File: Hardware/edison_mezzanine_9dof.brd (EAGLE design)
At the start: 30.5 x 44.5 mm, 43 parts, among them U1 LSM9DS0, U2 EDISON_CONNECTOR_FULLMOUNTING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, U3 EDISON_CONNECTOR_FULLHEADER, U4 MIC52053.3V

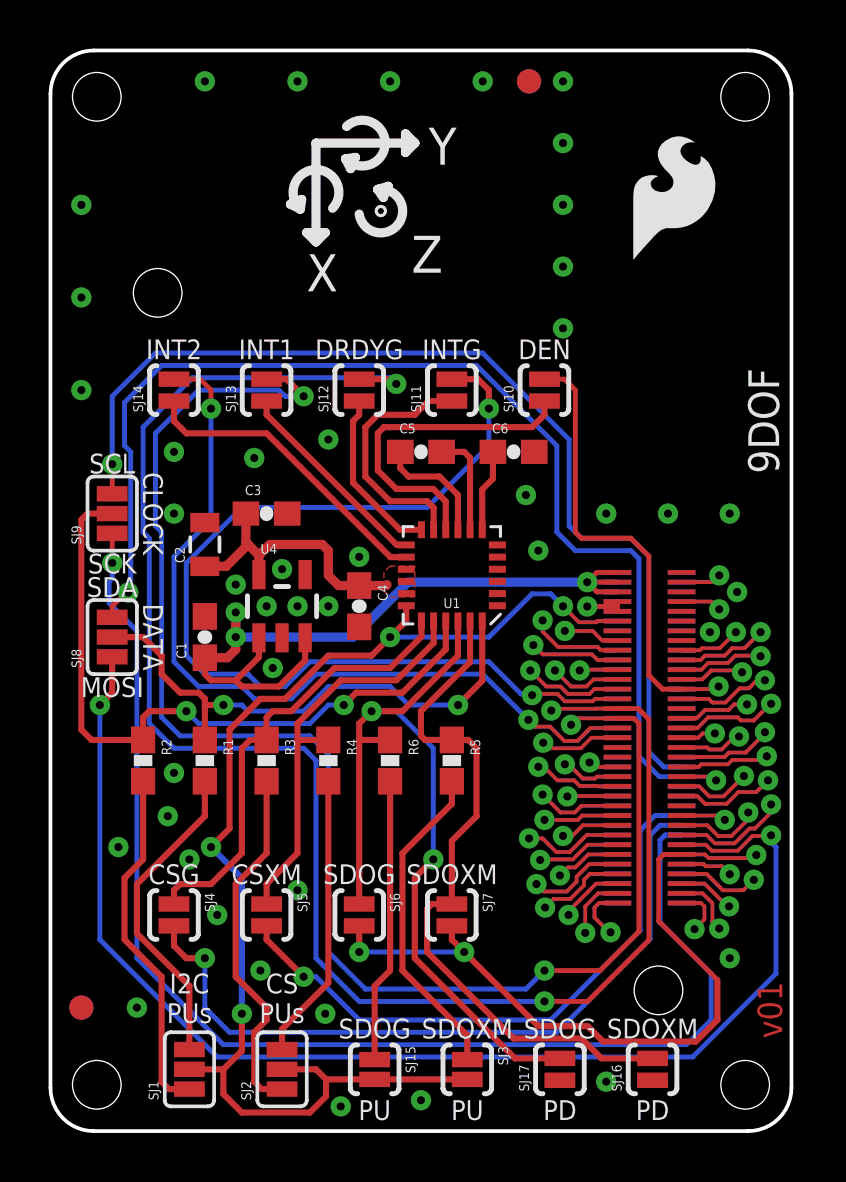
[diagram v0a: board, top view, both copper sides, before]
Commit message: Added DCIN pin Corrected Header footprint Modified Name of board cleaned up units and added units cleaned up copper fills
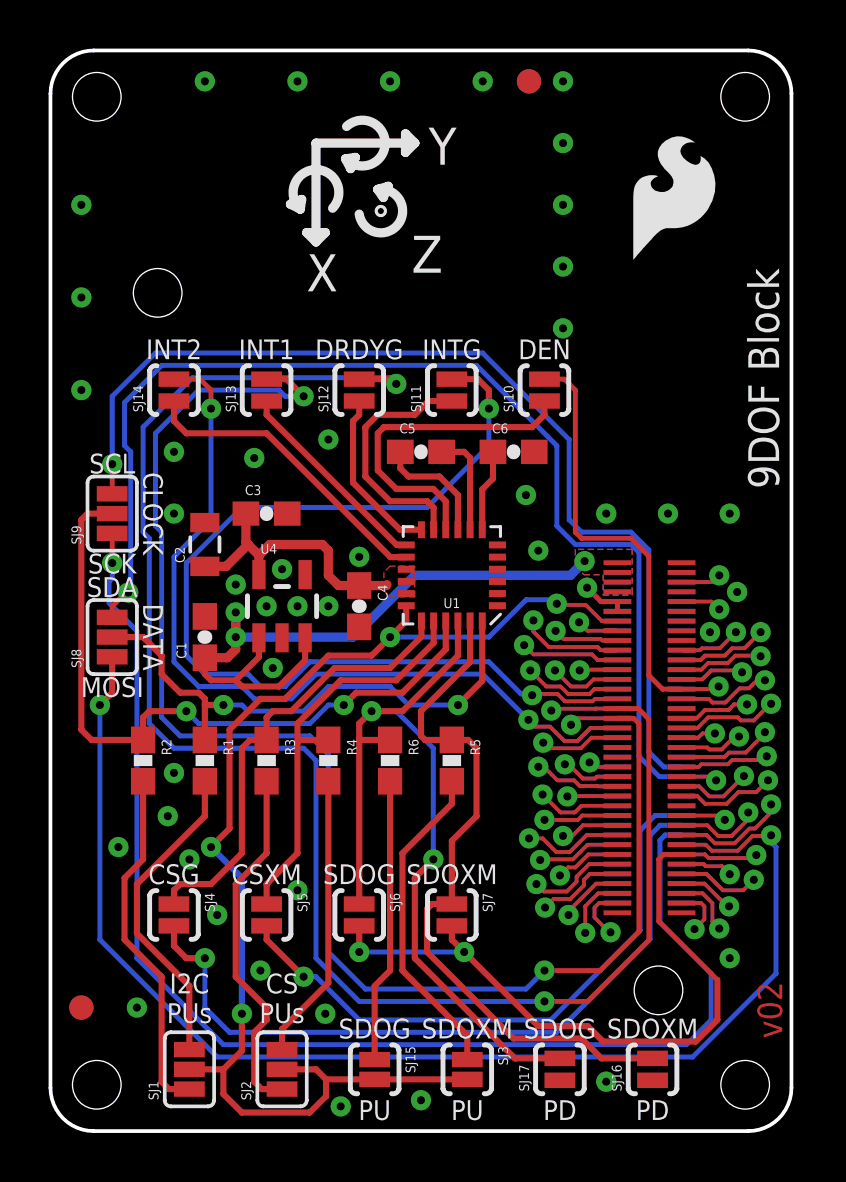
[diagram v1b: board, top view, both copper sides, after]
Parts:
- removed FRAME3: FRAME-LETTER, SparkFun-Aesthetics:CREATIVE_COMMONS
- R1, R2: value 4.7k -> DNP
- moved FRAME1 10.2 mm to (0.00, -15.2)
- moved FRAME2 10.2 mm to (0.00, -15.2)
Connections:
- new net DCIN: U2.14, U3.14
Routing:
- net VSYS: track 36.1 -> 28.3 mm
- net DCIN: track 0.00 -> 3.44 mm, vias 0 -> 1
- net USB_DP: track 4.65 -> 5.41 mm
- net USB_VBUS: track 7.42 -> 8.18 mm
- net USB_DN: track 7.70 -> 8.47 mm
- added copper zone on layer 1, net VSYS
- added copper zone on layer 16, net VSYS
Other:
- board text added: "9DOF Block"
- board text added: "NOTE: Units are in Inches"
- board text added: "v02"
- board text removed: "9DOF"
- board text removed: "Connectors Go Here"
- board text removed: "LED's and selector switches go here"
- board text removed: "Max Board Length"
- board text removed: "Nothing goes here... I mean it."
- board text removed: "v01"

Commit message: Rev to 10, fix gnd and pwr, text
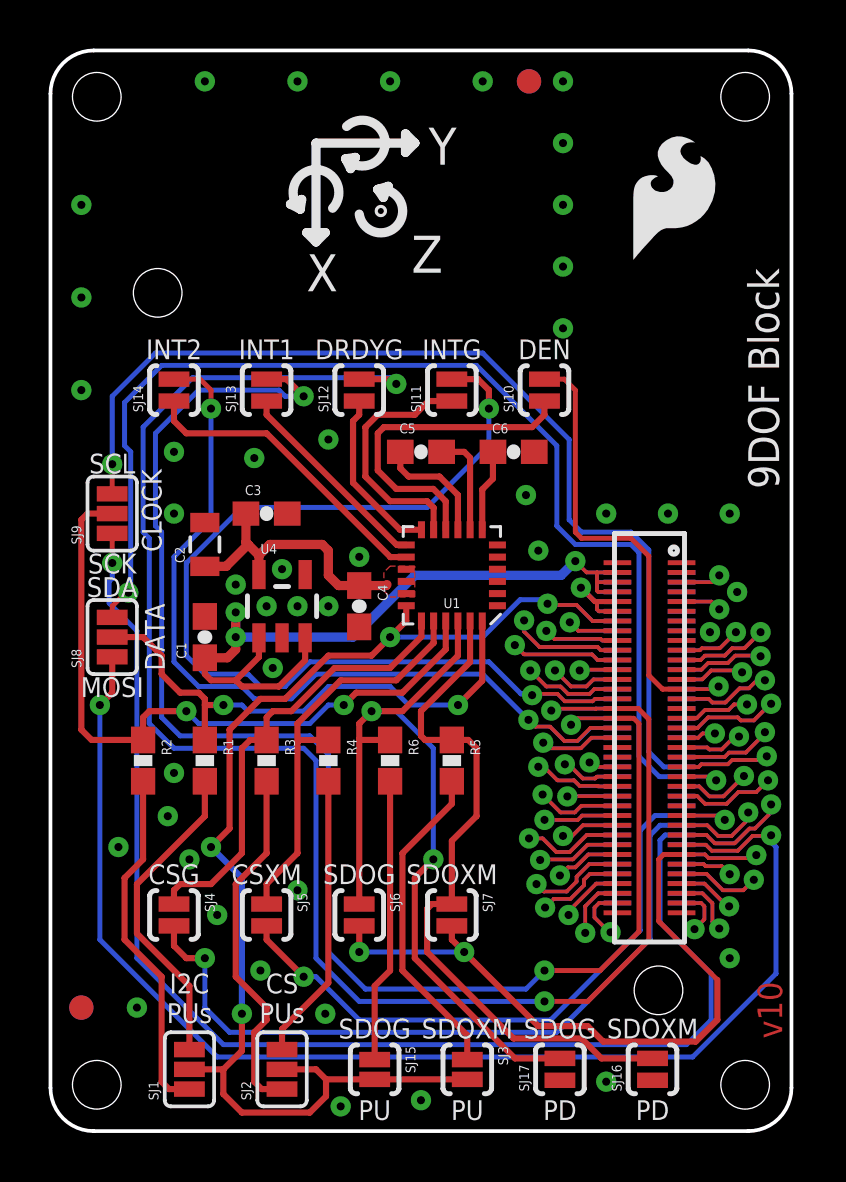
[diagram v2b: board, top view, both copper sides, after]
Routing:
- net VSYS: track 28.3 -> 36.7 mm
- net 3.3V: track 4.17 -> 5.97 mm
- net USB_VBUS: track 8.18 -> 8.94 mm
- net USB_DN: track 8.47 -> 9.23 mm
- net DCIN: track 3.44 -> 4.21 mm
- net USB_DP: track 5.41 -> 6.17 mm
- removed copper zone on layer 1, net VSYS
- removed copper zone on layer 16, net VSYS
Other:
- board text added: "v10"
- board text removed: "v02"

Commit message: Paste to trace jumpers, edit packages
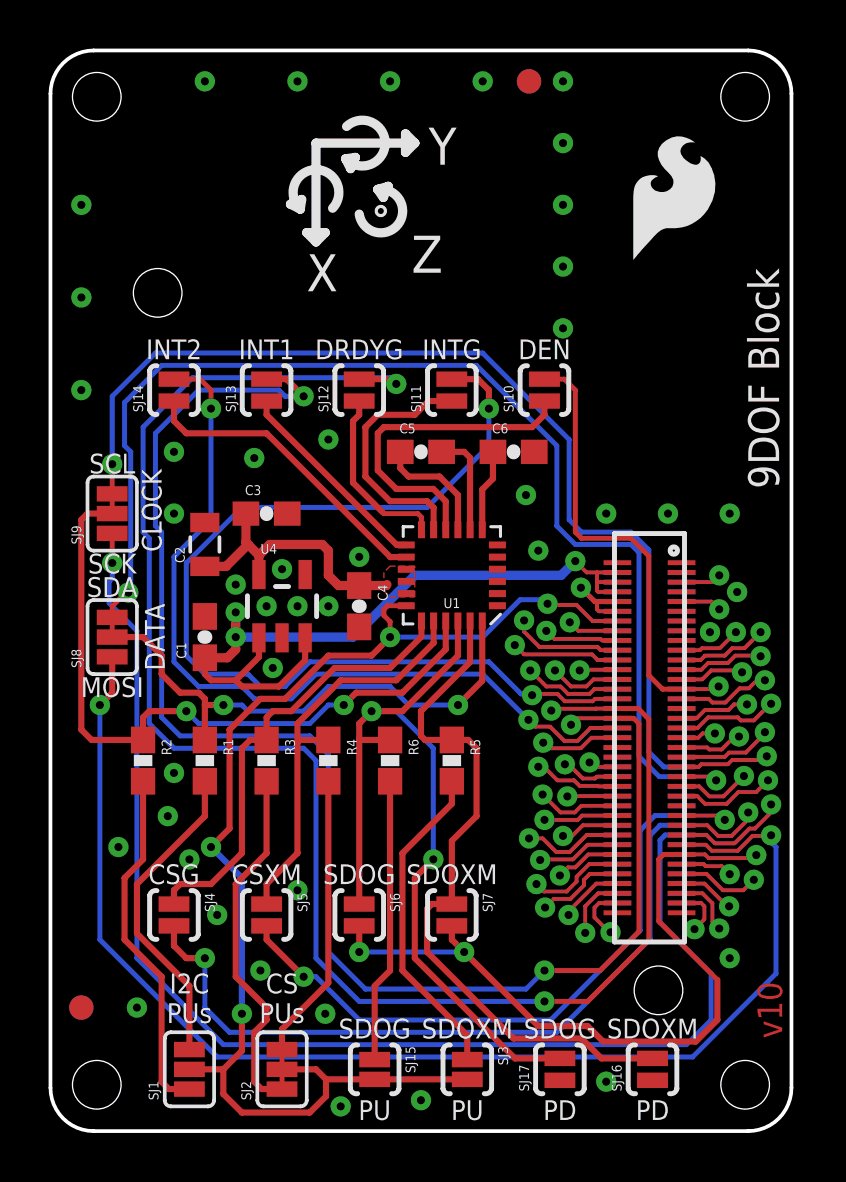
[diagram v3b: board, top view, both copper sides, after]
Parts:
- R1, R2: value DNP -> 10K
- SJ1: value JUMPER-PAD-3-NC_BY_PASTE -> JUMPER-PAD-3-NOYES_SILK; device SparkFun-Passives:PAD-JUMPER-3-NC_BY_PASTE_YES_SILK_FULL_BOX -> SparkFun-Passives:PAD-JUMPER-3-NO_YES_SILK
- SJ2: value JUMPER-PAD-3-NC_BY_PASTE -> (none); device SparkFun-Passives:PAD-JUMPER-3-NC_BY_PASTE_YES_SILK_FULL_BOX -> SparkFun-Passives:PAD-JUMPER-3-3OF3_NC_BY_TRACE_YES_SILK_FULL_BOX
- SJ8, SJ9: value JUMPER-PAD-3-2OF3_NC_BY_PASTE -> JUMPER-PAD-3-2OF3_NC_BY_TRACE_SMALL; device SparkFun-Passives:PAD-JUMPER-3-2OF3_NC_BY_PASTE_YES_SILK_FULL_BOX -> SparkFun-Passives:PAD-JUMPER-3-2OF3_NC_BY_TRACE_YES_SILK_FULL_BOX
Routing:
- net 1.8V: track 54.1 -> 54.8 mm
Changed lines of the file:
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@@
 <layer number="2" name="Route2" color="1" fill="3" visible="no" active="yes"/>
 <layer number="15" name="Route15" color="4" fill="6" visible="no" active="yes"/>
-<layer number="16" name="Bottom" color="1" fill="1" visible="no" active="yes"/>
+<layer number="16" name="Bottom" color="1" fill="1" visible="yes" active="yes"/>
 <layer number="17" name="Pads" color="2" fill="1" visible="yes" active="yes"/>
 <layer number="18" name="Vias" color="2" fill="1" visible="yes" active="yes"/>
@@
 <layer number="39" name="tKeepout" color="4" fill="11" visible="no" active="yes"/>
 <layer number="40" name="bKeepout" color="1" fill="11" visible="no" active="yes"/>
-<layer number="41" name="tRestrict" color="4" fill="10" visible="no" active="yes"/>
+<layer number="41" name="tRestrict" color="4" fill="10" visible="yes" active="yes"/>
 <layer number="42" name="bRestrict" color="1" fill="10" visible="no" active="yes"/>
 <layer number="43" name="vRestrict" color="2" fill="10" visible="no" active="yes"/>
@@
 <text x="33.02" y="-2.54" size="1.778" layer="51">NOTE: Units are in Inches</text>
 <text x="29.972" y="37.338" size="1.27" layer="22" font="vector" ratio="15" rot="SMR270">9DOF Block</text>
+<wire x1="18.288" y1="23.876" x2="18.542" y2="23.876" width="0.1524" layer="41"/>
+<wire x1="18.288" y1="23.368" x2="18.542" y2="23.368" width="0.1524" layer="41"/>
+<wire x1="18.288" y1="22.86" x2="18.542" y2="22.86" width="0.1524" layer="41"/>
+<wire x1="18.288" y1="22.352" x2="18.542" y2="22.352" width="0.1524" layer="41"/>
+<wire x1="14.732" y1="22.352" x2="14.478" y2="22.352" width="0.1524" layer="41"/>
+<wire x1="14.732" y1="22.86" x2="14.478" y2="22.86" width="0.1524" layer="41"/>
+<wire x1="18.288" y1="24.384" x2="18.542" y2="24.384" width="0.1524" layer="41"/>
 </plain>
 <attributes>
@@
 <attribute name="PROD_ID" value="CAP-00868" x="5.08" y="38.1" size="1.778" layer="27" font="vector" ratio="15" display="off"/>
 </element>
-<element name="R1" library="SparkFun-Resistors" package="0603-RES" value="DNP" x="6.35" y="15.24" rot="R270">
+<element name="R1" library="SparkFun-Resistors" package="0603-RES" value="10K" x="6.35" y="15.24" rot="R270">
 <attribute name="PROD_ID" value="RES-00824" x="15.24" y="22.86" size="1.778" layer="27" font="vector" ratio="15" rot="R270" display="off"/>
 </element>
-<element name="R2" library="SparkFun-Resistors" package="0603-RES" value="DNP" x="3.81" y="15.24" rot="R270">
+<element name="R2" library="SparkFun-Resistors" package="0603-RES" value="10K" x="3.81" y="15.24" rot="R270">
 <attribute name="PROD_ID" value="RES-00824" x="8.89" y="26.67" size="1.778" layer="27" font="vector" ratio="15" rot="R270" display="off"/>
 </element>
@@
 <element name="SJ13" library="SparkFun-Passives" package="PAD-JUMPER-2-NO_YES_SILK" value="JUMPER-PAD-2-NOYES_SILK" x="8.89" y="30.48" rot="R90"/>
 <element name="SJ14" library="SparkFun-Passives" package="PAD-JUMPER-2-NO_YES_SILK" value="JUMPER-PAD-2-NOYES_SILK" x="5.08" y="30.48" rot="R90"/>
-<element name="SJ8" library="SparkFun-Passives" package="PAD-JUMPER-3-2OF3_NC_BY_PASTE_YES_SILK_FULL_BOX" value="JUMPER-PAD-3-2OF3_NC_BY_PASTE" x="2.54" y="20.32" rot="R90"/>
-<element name="SJ9" library="SparkFun-Passives" package="PAD-JUMPER-3-2OF3_NC_BY_PASTE_YES_SILK_FULL_BOX" value="JUMPER-PAD-3-2OF3_NC_BY_PASTE" x="2.54" y="25.4" rot="R90"/>
-<element name="SJ2" library="SparkFun-Passives" package="PAD-JUMPER-3-NC_BY_PASTE_YES_SILK_FULL_BOX" value="JUMPER-PAD-3-NC_BY_PASTE" x="9.525" y="2.54" rot="R90"/>
-<element name="SJ1" library="SparkFun-Passives" package="PAD-JUMPER-3-NC_BY_PASTE_YES_SILK_FULL_BOX" value="JUMPER-PAD-3-NC_BY_PASTE" x="5.715" y="2.54" rot="R90"/>
+<element name="SJ8" library="SparkFun-Passives" package="PAD-JUMPER-3-2OF3_NC_BY_TRACE_YES_SILK_FULL_BOX" value="JUMPER-PAD-3-2OF3_NC_BY_TRACE_SMALL" x="2.54" y="20.32" rot="R90"/>
+<element name="SJ9" library="SparkFun-Passives" package="PAD-JUMPER-3-2OF3_NC_BY_TRACE_YES_SILK_FULL_BOX" value="JUMPER-PAD-3-2OF3_NC_BY_TRACE_SMALL" x="2.54" y="25.4" rot="R90"/>
+<element name="SJ2" library="SparkFun-Passives" package="PAD-JUMPER-3-3OF3_NC_BY_TRACE_YES_SILK_FULL_BOX" value="" x="9.525" y="2.54" rot="R90"/>
+<element name="SJ1" library="SparkFun-Passives" package="PAD-JUMPER-3-NO_YES_SILK" value="JUMPER-PAD-3-NOYES_SILK" x="5.715" y="2.54" rot="R90"/>
 <element name="U4" library="SparkFun-PowerIC" package="SOT23-5" value="MIC52053.3V" x="9.525" y="21.59">
 <attribute name="PROD_ID" value="VREG-00822" x="9.525" y="21.59" size="1.778" layer="27" font="vector" ratio="15" display="off"/>
@@
 <wire x1="11.43" y1="19.558" x2="13.208" y2="19.558" width="0.254" layer="1"/>
 <wire x1="13.208" y1="19.558" x2="13.97" y2="20.32" width="0.254" layer="1"/>
-<wire x1="14.635" y1="21.61" x2="14.635" y2="20.985" width="0.254" layer="1"/>
-<wire x1="14.635" y1="20.985" x2="13.97" y2="20.32" width="0.254" layer="1"/>
 <wire x1="19.3167" y1="21.8567" x2="17.78" y2="20.32" width="0.2032" layer="16"/>
 <wire x1="17.78" y1="20.32" x2="13.97" y2="20.32" width="0.2032" layer="16"/>
@@
 <wire x1="20.447" y1="21.6916" x2="20.2819" y2="21.8567" width="0.2032" layer="16"/>
 <wire x1="20.2819" y1="21.8567" x2="19.3167" y2="21.8567" width="0.2032" layer="16"/>
+<wire x1="14.635" y1="21.61" x2="13.863" y2="21.61" width="0.2032" layer="1"/>
+<wire x1="13.863" y1="21.61" x2="13.716" y2="21.463" width="0.2032" layer="1"/>
+<wire x1="13.716" y1="21.463" x2="13.716" y2="21.209" width="0.2032" layer="1"/>
+<wire x1="13.716" y1="21.209" x2="13.97" y2="20.955" width="0.2032" layer="1"/>
+<wire x1="13.97" y1="20.955" x2="13.97" y2="20.32" width="0.2032" layer="1"/>
 </signal>
 <signal name="FW_RCVR">
@@
 <contactref element="U1" pad="12"/>
 <contactref element="SJ12" pad="1"/>
-<wire x1="15.26" y1="24.735" x2="14.381" y2="24.735" width="0.254" layer="1"/>
-<wire x1="14.381" y1="24.735" x2="12.446" y2="26.67" width="0.254" layer="1"/>
+<wire x1="13.6525" y1="25.4635" x2="12.446" y2="26.67" width="0.254" layer="1"/>
 <wire x1="12.7" y1="30.03" x2="12.7" y2="29.464" width="0.254" layer="1"/>
 <wire x1="12.7" y1="29.464" x2="12.446" y2="29.21" width="0.254" layer="1"/>
 <wire x1="12.446" y1="29.21" x2="12.446" y2="26.67" width="0.254" layer="1"/>
+<wire x1="15.26" y1="24.735" x2="15.26" y2="25.253" width="0.2032" layer="1"/>
+<wire x1="15.26" y1="25.253" x2="15.113" y2="25.4" width="0.2032" layer="1"/>
+<wire x1="15.113" y1="25.4" x2="13.716" y2="25.4" width="0.2032" layer="1"/>
+<wire x1="13.716" y1="25.4" x2="13.6525" y2="25.4635" width="0.2032" layer="1"/>
 </signal>
 <signal name="INT_G">
@@
 <contactref element="C3" pad="1"/>
 <contactref element="C4" pad="1"/>
-<polygon width="0.1778" layer="1" isolate="0.2032" rank="2">
+<polygon width="0.1778" layer="1" isolate="0.0508" rank="2">
 <vertex x="14.986" y="23.241"/>
 <vertex x="13.97" y="23.241"/>
@@
 </signal>
 </signals>
+<errors>
+</errors>
 </board>
 </drawing>
